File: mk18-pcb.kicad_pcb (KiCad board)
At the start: 2 copper layers, 128.2 x 70 mm, 59 parts, among them U2 AZC199-04S-MS, U3 1N4148W_C81598, U4 1N4148W_C81598, U5 1N4148W_C81598, U6 1N4148W_C81598, U7 1N4148W_C81598

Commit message: added debug, test points, more
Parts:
- added DBG1: Conn_01x03_Socket, Connector_JST:JST_EH_B3B-EH-A_1x03_P2.50mm_Vertical, F.Cu at (111.7, 133.8)
- added T1: Conn_01x01_Socket, Connector_Pin:Pin_D1.0mm_L10.0mm, F.Cu at (116.3, 132.9)
- added T10: Conn_01x01_Socket, Connector_Pin:Pin_D1.0mm_L10.0mm, F.Cu at (120.5, 76.8)
- added T2: Conn_01x01_Socket, Connector_Pin:Pin_D1.0mm_L10.0mm, F.Cu at (129.7, 135.2)
- added T3: Conn_01x01_Socket, Connector_Pin:Pin_D1.0mm_L10.0mm, F.Cu at (119.5, 134.9)
- added T4: Conn_01x01_Socket, Connector_Pin:Pin_D1.0mm_L10.0mm, F.Cu at (116.3, 128.2)
- added T5: Conn_01x01_Socket, Connector_Pin:Pin_D1.0mm_L10.0mm, F.Cu at (123.6, 76.8)
- added T6: Conn_01x01_Socket, Connector_Pin:Pin_D1.0mm_L10.0mm, F.Cu at (199.8, 83.0)
- added T7: Conn_01x01_Socket, Connector_Pin:Pin_D1.0mm_L10.0mm, F.Cu at (196.5, 83.0)
- added T8: Conn_01x01_Socket, Connector_Pin:Pin_D1.0mm_L10.0mm, F.Cu at (176.9, 99.4)
- added T9: Conn_01x01_Socket, Connector_Pin:Pin_D1.0mm_L10.0mm, F.Cu at (125.5, 82.9)
- moved LED-MACRO1 1.66 mm to (181.4, 99.5)
- moved LED-FAL1 1.30 mm to (187.2, 102.0)
- moved LED-FAL2 0.83 mm to (194.2, 99.5)
- moved LED-IND1 0.36 mm to (199.9, 102.0)
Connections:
- net /LED_DI_3.3V renamed LED_DI_3.3V
- PICO1 pad 41: unconnected-(PICO1-SWCLK-Pad41) -> SWCLK
- PICO1 pad 42: unconnected-(PICO1-GND-Pad42) -> SWGND
- PICO1 pad 43: unconnected-(PICO1-SWDIO-Pad43) -> SWDIO
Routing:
- net SWCLK: track 0.00 -> 72.2 mm, vias 0 -> 2
- net SWGND: track 0.00 -> 71.2 mm, vias 0 -> 2
- net SWDIO: track 0.00 -> 70.8 mm, vias 0 -> 2
- net Split_Comms_TX: track 51.5 -> 69.6 mm
- net LED_KEYS_DI: track 75.9 -> 86.2 mm, vias 2 -> 3
- net LED_DI_3.3V: track 11.1 -> 20.2 mm
- net COL_CS_MOS: track 41.5 -> 46.7 mm
- net SPI1_MOSI: track 124.8 -> 129.2 mm
- net Split_Comms_RX: track 55.7 -> 59.8 mm
- net COL_CS: track 52.2 -> 56.1 mm
- net SPI1_MISO: track 179.4 -> 183.1 mm, vias 6 -> 7
- net +3V3: track 355.6 -> 358.9 mm
- net LED_KEYS_DO: track 91.7 -> 94.9 mm
- net SPI1_CLK: track 243.6 -> 246.0 mm
- net ROW_CS: track 82.5 -> 84.7 mm
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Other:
- board size 128.2 x 70 mm -> 128.2 x 75 mm

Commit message: preparing to redo some parts
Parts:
- added G***: LOGO, ct-kicad:awesome-logo, F.Cu at (210.0, 139.8)
- added G***: LOGO, ct-kicad:awesome-logo, B.Cu at (107.0, 140.0)
- moved H3 7.95 mm to (100.2, 139.7)
- moved H4 5.70 mm to (217.9, 139.4)
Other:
- outline, holes or cut-outs redrawn
- board text added: "ArcBoard mk19"

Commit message: before updating the macropad connector
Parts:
- removed H5: MountingHole, MountingHole:MountingHole_3.2mm_M3
- added LOGO1: QMK Logo, ct-kicad:QMK_PoweredBy, F.Cu at (217.9, 118.8)
- added LOGO1: QMK Logo, ct-kicad:QMK_PoweredBy, B.Cu at (217.9, 118.8)
- H1, H2, H3, H4: footprint MountingHole:MountingHole_3.2mm_M3 -> MountingHole:MountingHole_3.2mm_M3_Pad_Via
- moved G*** 103.8 mm to (210.6, 134.2)
- moved H2 40.2 mm to (217.7, 75.9)
- moved G*** 5.60 mm to (210.6, 134.2)
- moved RESET1 2.89 mm to (215.8, 99.5), turned to -90 degrees
- moved LED-IND1 2.61 mm to (200.6, 99.5), turned to -90 degrees
- moved LED-FAL1 2.57 mm to (187.8, 99.5), turned to -90 degrees
- moved HAND1 0.15 mm to (143.7, 79.0)
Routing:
- net LED_FAL1_DI: track 91.8 -> 95.0 mm
- net LED_FAL1_DO: track 37.1 -> 35.2 mm
- net LED_FAL2_DO: track 29.9 -> 31.7 mm
- net LED_INDICATORS_DO: track 56.1 -> 55.1 mm
- net GND: vias 193 -> 194
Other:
- board text added: "0 -> 7"
- board text added: "1 2 FALCONS"
- board text added: "15 <- 8"
- board text added: "5 3.3 G"
- board text added: "589 REGISTERS COL1 COL2"
- board text added: "7 <- 0"
- board text added: "8 -> 15"
- board text added: "ADC"
- board text added: "CYBOARD"
- board text added: "DPAD"
- board text added: "Debug"
- board text added: "G27 G26 AGD"
- board text added: "HAND R L"
- board text added: "INDs"
- board text added: "LCD"
- board text added: "MACRO"
- board text added: "PMW"
- board text added: "POWER"
- board text added: "RESET"
- board text added: "ROW1 595 REGISTERS ROW2"
- board text added: "TO SCREEN INDs"
- board text removed: "-->"
- board text removed: "Cyboard Main"
- board text removed: "FAL1"
- board text removed: "FAL2"
- board text removed: "IND1"
- board text removed: "Macropad"
- board text removed: "TO SCREEN IND's"

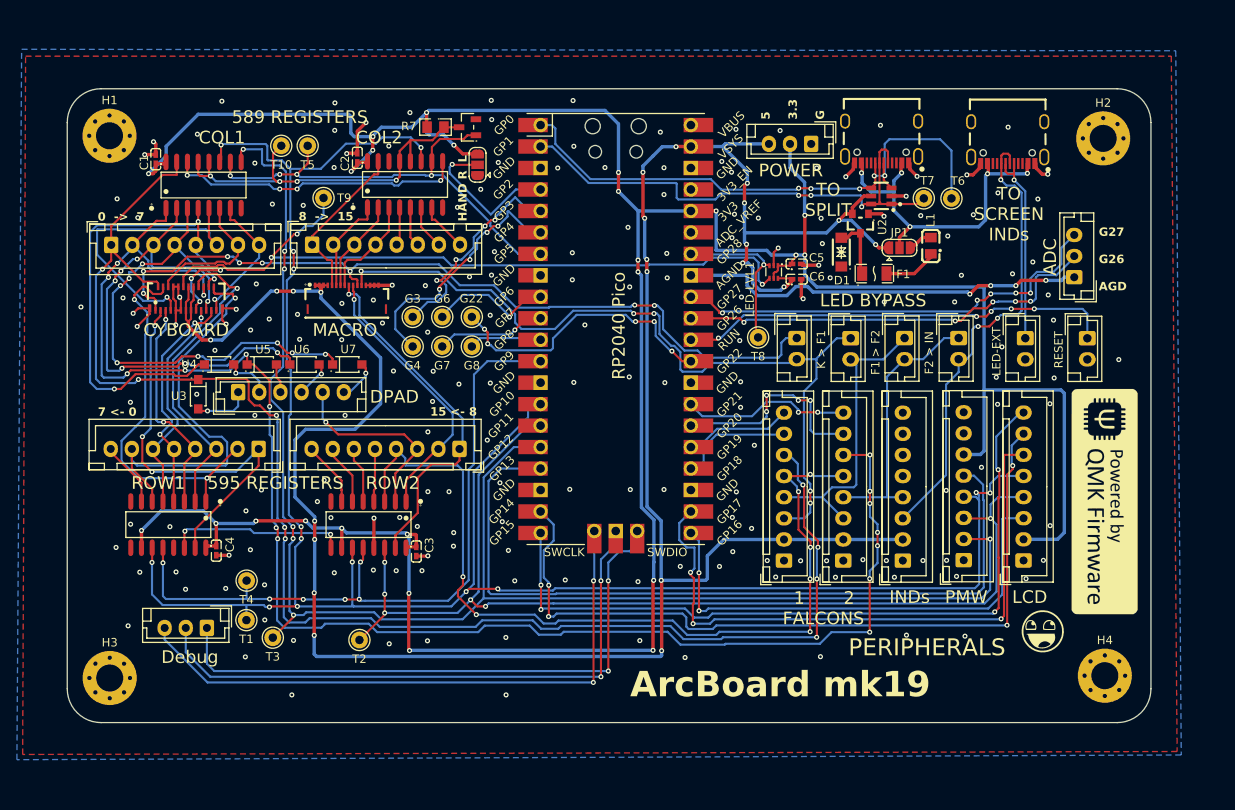
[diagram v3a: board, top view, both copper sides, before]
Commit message: replace two parts
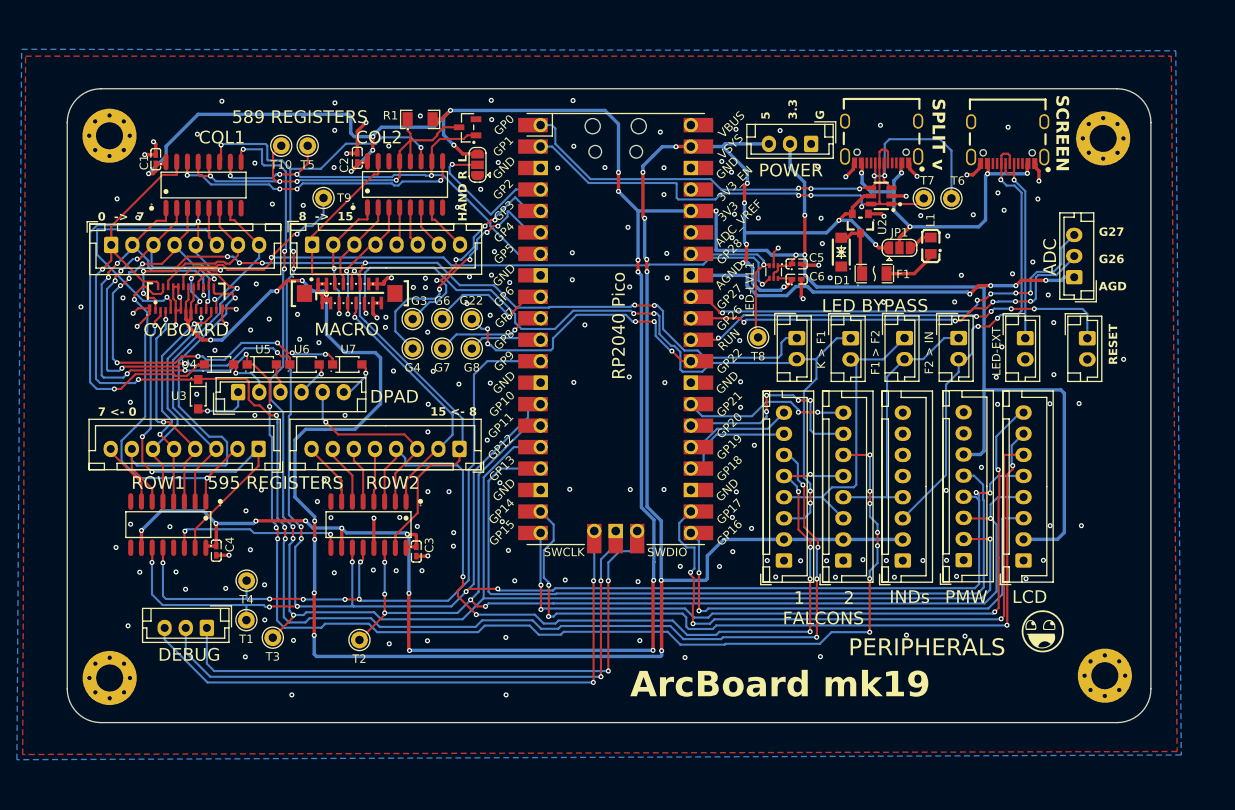
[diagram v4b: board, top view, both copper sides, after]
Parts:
- removed LOGO1 (x2): QMK Logo, ct-kicad:QMK_PoweredBy
- removed R7: RK73H2ATTD9101F, ct-kicad:R0805
- added R1: 1206W4F1002T5E, ct-kicad:R1206, F.Cu at (136.9, 73.6)
- CYBOARD-MACRO1: footprint ct-kicad:FPC-SMD_16P-P0.50_HCTL_HC-FPC-05-10-16RLTAG -> ct-kicad:FPC-SMD_16P-P0.50_HDGC_0.5K-A-16PBF
- moved CYBOARD-MACRO1 0.56 mm to (128.6, 94.2), turned to 0 degrees
- moved G22 0.25 mm to (143.0, 97.2)
- moved G3 0.25 mm to (136.0, 97.2)
- moved G4 0.25 mm to (136.0, 100.8)
- moved G6 0.25 mm to (139.5, 97.2)
- moved G7 0.25 mm to (139.5, 100.8)
- moved G8 0.25 mm to (143.0, 100.8)
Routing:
- net VCC: track 284.6 -> 292.4 mm
- net col9: track 11.6 -> 16.9 mm, vias 0 -> 2
- net LED_FAL1_DI: track 95.0 -> 99.4 mm
- net col11: track 12.3 -> 16.4 mm, vias 0 -> 2
- net GND: track 54.4 -> 57.8 mm, vias 194 -> 199
- net COL_CS_MOS: track 46.7 -> 49.3 mm
- net row8: track 42.1 -> 44.7 mm
- net row9: track 32.8 -> 30.7 mm
- net col8: track 19.4 -> 20.6 mm
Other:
- board text added: "DEBUG"
- board text added: "SCREEN"
- board text added: "SPLIT v"
- board text removed: "Debug"
- board text removed: "TO SCREEN INDs"
- board text removed: "TO SPLIT"
